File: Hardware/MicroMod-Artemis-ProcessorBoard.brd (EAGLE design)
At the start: 22 x 22 mm, 40 parts, among them J1 MICROMOD-2222, U1 ARTEMIS_MODULESMD, U2 TSV524, U6 CH340E_MSOP10, Y1 32.768kHz

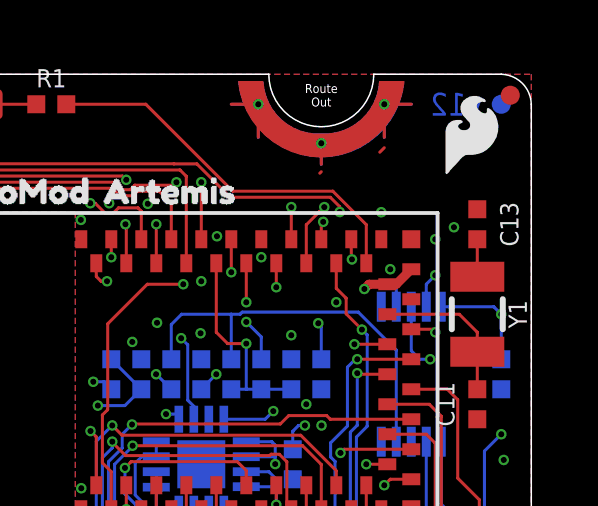
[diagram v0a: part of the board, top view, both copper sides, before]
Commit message: Add missing net to Xtal
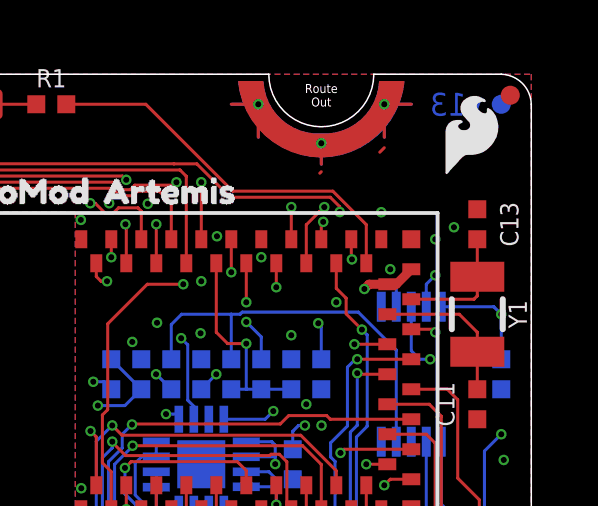
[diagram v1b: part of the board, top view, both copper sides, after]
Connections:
- removed net N$4: U1.XI
- net N$5: now also U1.XI
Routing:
- net N$5: track 1.25 -> 4.13 mm
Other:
- board text added: "v13"
- board text removed: "v12"
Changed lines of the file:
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@@
 <?xml version="1.0" encoding="utf-8"?>
 <!DOCTYPE eagle SYSTEM "eagle.dtd">
-<eagle version="9.6.0">
+<eagle version="9.6.2">
 <drawing>
 <settings>
@@
 <setting verticaltext="up"/>
 </settings>
-<grid distance="0.05" unitdist="inch" unit="inch" style="lines" multiple="1" display="yes" altdistance="0.05" altunitdist="mm" altunit="mm"/>
+<grid distance="0.05" unitdist="inch" unit="inch" style="lines" multiple="1" display="yes" altdistance="0.005" altunitdist="inch" altunit="inch"/>
 <layers>
 <layer number="1" name="Top" color="4" fill="1" visible="yes" active="yes"/>
-<layer number="2" name="Horz" color="1" fill="3" visible="yes" active="yes"/>
-<layer number="15" name="Vert" color="4" fill="6" visible="yes" active="yes"/>
+<layer number="2" name="Horz" color="1" fill="3" visible="no" active="yes"/>
+<layer number="15" name="Vert" color="4" fill="6" visible="no" active="yes"/>
 <layer number="16" name="Bottom" color="1" fill="1" visible="yes" active="yes"/>
 <layer number="17" name="Pads" color="2" fill="1" visible="yes" active="yes"/>
@@
 <layer number="23" name="tOrigins" color="15" fill="1" visible="yes" active="yes"/>
 <layer number="24" name="bOrigins" color="15" fill="1" visible="yes" active="yes"/>
-<layer number="25" name="tNames" color="7" fill="1" visible="yes" active="yes"/>
-<layer number="26" name="bNames" color="7" fill="1" visible="yes" active="yes"/>
-<layer number="27" name="tValues" color="7" fill="1" visible="yes" active="yes"/>
-<layer number="28" name="bValues" color="7" fill="1" visible="yes" active="yes"/>
-<layer number="29" name="tStop" color="7" fill="3" visible="yes" active="yes"/>
-<layer number="30" name="bStop" color="7" fill="6" visible="yes" active="yes"/>
-<layer number="31" name="tCream" color="7" fill="4" visible="yes" active="yes"/>
-<layer number="32" name="bCream" color="7" fill="5" visible="yes" active="yes"/>
-<layer number="33" name="tFinish" color="6" fill="3" visible="yes" active="yes"/>
-<layer number="34" name="bFinish" color="6" fill="6" visible="yes" active="yes"/>
-<layer number="35" name="tGlue" color="7" fill="4" visible="yes" active="yes"/>
-<layer number="36" name="bGlue" color="7" fill="5" visible="yes" active="yes"/>
-<layer number="37" name="tTest" color="7" fill="1" visible="yes" active="yes"/>
-<layer number="38" name="bTest" color="7" fill="1" visible="yes" active="yes"/>
-<layer number="39" name="tKeepout" color="4" fill="11" visible="yes" active="yes"/>
-<layer number="40" name="bKeepout" color="1" fill="11" visible="yes" active="yes"/>
-<layer number="41" name="tRestrict" color="4" fill="10" visible="yes" active="yes"/>
-<layer number="42" name="bRestrict" color="1" fill="10" visible="yes" active="yes"/>
-<layer number="43" name="vRestrict" color="2" fill="10" visible="yes" active="yes"/>
-<layer number="44" name="Drills" color="7" fill="1" visible="yes" active="yes"/>
+<layer number="25" name="tNames" color="7" fill="1" visible="no" active="yes"/>
+<layer number="26" name="bNames" color="7" fill="1" visible="no" active="yes"/>
+<layer number="27" name="tValues" color="7" fill="1" visible="no" active="yes"/>
+<layer number="28" name="bValues" color="7" fill="1" visible="no" active="yes"/>
+<layer number="29" name="tStop" color="7" fill="3" visible="no" active="yes"/>
+<layer number="30" name="bStop" color="7" fill="6" visible="no" active="yes"/>
+<layer number="31" name="tCream" color="7" fill="4" visible="no" active="yes"/>
+<layer number="32" name="bCream" color="7" fill="5" visible="no" active="yes"/>
+<layer number="33" name="tFinish" color="6" fill="3" visible="no" active="yes"/>
+<layer number="34" name="bFinish" color="6" fill="6" visible="no" active="yes"/>
+<layer number="35" name="tGlue" color="7" fill="4" visible="no" active="yes"/>
+<layer number="36" name="bGlue" color="7" fill="5" visible="no" active="yes"/>
+<layer number="37" name="tTest" color="7" fill="1" visible="no" active="yes"/>
+<layer number="38" name="bTest" color="7" fill="1" visible="no" active="yes"/>
+<layer number="39" name="tKeepout" color="4" fill="11" visible="no" active="yes"/>
+<layer number="40" name="bKeepout" color="1" fill="11" visible="no" active="yes"/>
+<layer number="41" name="tRestrict" color="4" fill="10" visible="no" active="yes"/>
+<layer number="42" name="bRestrict" color="1" fill="10" visible="no" active="yes"/>
+<layer number="43" name="vRestrict" color="2" fill="10" visible="no" active="yes"/>
+<layer number="44" name="Drills" color="7" fill="1" visible="no" active="yes"/>
 <layer number="45" name="Holes" color="7" fill="1" visible="yes" active="yes"/>
-<layer number="46" name="Milling" color="3" fill="1" visible="yes" active="yes"/>
-<layer number="47" name="Measures" color="7" fill="1" visible="yes" active="yes"/>
-<layer number="48" name="Document" color="7" fill="1" visible="yes" active="yes"/>
-<layer number="49" name="Reference" color="7" fill="1" visible="yes" active="yes"/>
-<layer number="50" name="dxf" color="7" fill="1" visible="yes" active="yes"/>
+<layer number="46" name="Milling" color="3" fill="1" visible="no" active="yes"/>
+<layer number="47" name="Measures" color="7" fill="1" visible="no" active="yes"/>
+<layer number="48" name="Document" color="7" fill="1" visible="no" active="yes"/>
+<layer number="49" name="Reference" color="7" fill="1" visible="no" active="yes"/>
+<layer number="50" name="dxf" color="7" fill="1" visible="no" active="yes"/>
 <layer number="51" name="tDocu" color="6" fill="1" visible="yes" active="yes"/>
-<layer number="52" name="bDocu" color="7" fill="1" visible="yes" active="yes"/>
+<layer number="52" name="bDocu" color="7" fill="1" visible="no" active="yes"/>
 <layer number="91" name="Nets" color="2" fill="1" visible="no" active="no"/>
 <layer number="92" name="Busses" color="1" fill="1" visible="no" active="no"/>
@@
 <wire x1="0" y1="4.6" x2="0.6" y2="4" width="0.05" layer="20" curve="86.784874"/>
 <rectangle x1="3.1" y1="6.6" x2="6.6" y2="17.3" layer="39"/>
-<text x="19.5" y="21" size="0.762" layer="16" font="vector" ratio="15" rot="SMR0" align="center">v12</text>
+<text x="19.5" y="21" size="0.762" layer="16" font="vector" ratio="15" rot="SMR0" align="center">v13</text>
 <text x="17.78" y="-8.89" size="1.778" layer="51" font="vector" ratio="15">N. Seidle</text>
 <wire x1="13.25" y1="22" x2="16.75" y2="22" width="0.05" layer="20" curve="180"/>
@@
 <wire x1="15.15594375" y1="3.7286" x2="15.8734" y2="4.44605625" width="0.1016" layer="16"/>
 </signal>
-<signal name="N$4">
-<contactref element="U1" pad="XI"/>
-</signal>
 <signal name="N$5">
 <contactref element="Y1" pad="P$1"/>
 <contactref element="C13" pad="2"/>
 <wire x1="20.2" y1="15.25" x2="20.2" y2="16.5" width="0.1016" layer="1"/>
-</signal>
-<signal name="N$6">
+<contactref element="U1" pad="XI"/>
+<wire x1="18" y1="14.5" x2="20.088" y2="14.5" width="0.1016" layer="1"/>
+<wire x1="20.2" y1="14.612" x2="20.2" y2="15.25" width="0.1016" layer="1"/>
+<wire x1="20.088" y1="14.5" x2="20.2" y2="14.612" width="0.1016" layer="1"/>
 </signal>
 <signal name="SCALED_BATT_VIN/3">

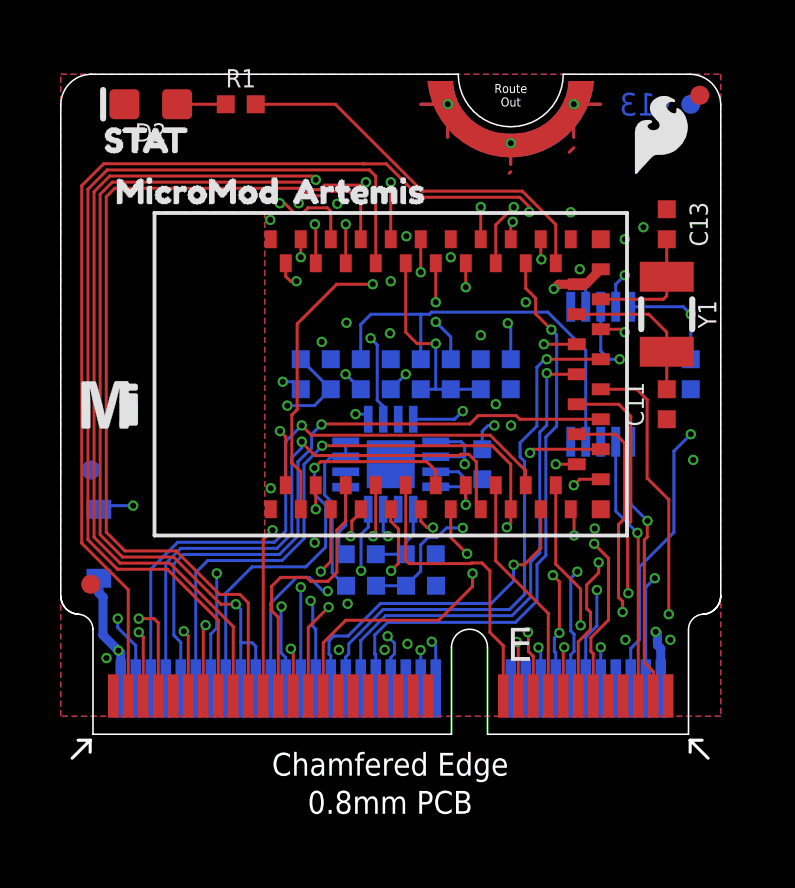
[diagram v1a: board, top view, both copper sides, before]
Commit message: Fix SDA1/SCL1, CS1, and VIN/3 incorrect pin locations.
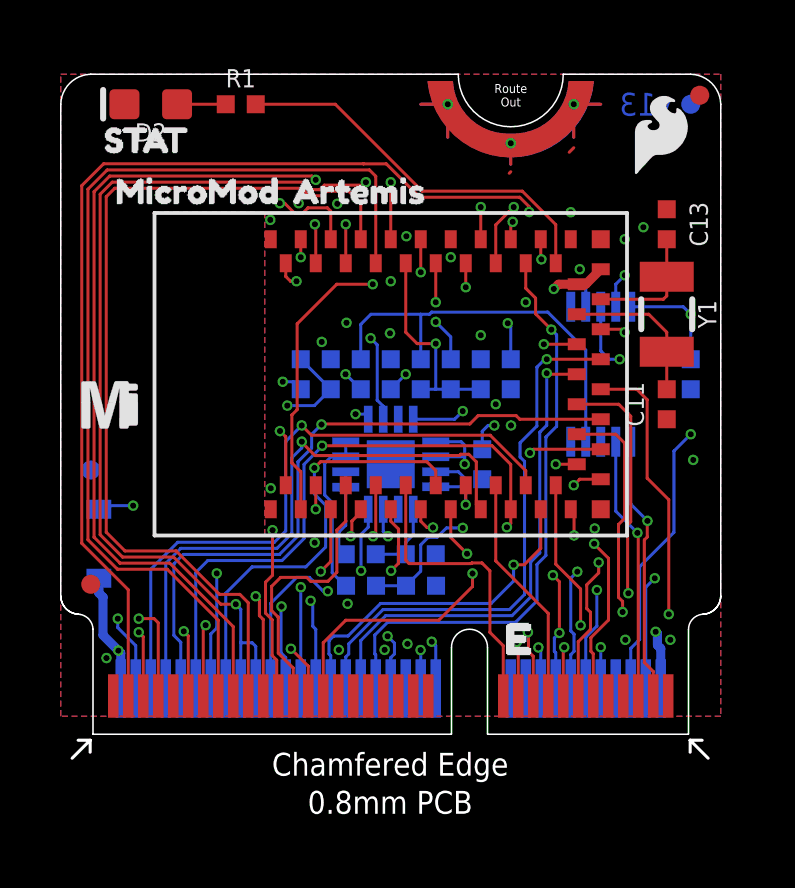
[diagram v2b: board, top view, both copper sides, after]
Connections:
- net BATT_VIN/3: now also J1.49; no longer J1.51
- net SCL1: now also J1.53; no longer J1.55
- net SDA1: now also J1.51; no longer J1.53
- net SPI_!CS!1: now also J1.55; no longer J1.49
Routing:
- net SPI_!CS!1: track 22.9 -> 28.2 mm
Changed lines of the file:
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@@
 <?xml version="1.0" encoding="utf-8"?>
 <!DOCTYPE eagle SYSTEM "eagle.dtd">
-<eagle version="9.6.2">
+<eagle version="9.6.0">
 <drawing>
 <settings>
@@
 <setting verticaltext="up"/>
 </settings>
-<grid distance="0.05" unitdist="inch" unit="inch" style="lines" multiple="1" display="yes" altdistance="0.005" altunitdist="inch" altunit="inch"/>
+<grid distance="1" unitdist="mm" unit="mm" style="lines" multiple="1" display="yes" altdistance="0.1" altunitdist="mm" altunit="mm"/>
 <layers>
 <layer number="1" name="Top" color="4" fill="1" visible="yes" active="yes"/>
 <layer number="2" name="Horz" color="1" fill="3" visible="no" active="yes"/>
-<layer number="15" name="Vert" color="4" fill="6" visible="no" active="yes"/>
+<layer number="15" name="Vert" color="4" fill="6" visible="yes" active="yes"/>
 <layer number="16" name="Bottom" color="1" fill="1" visible="yes" active="yes"/>
 <layer number="17" name="Pads" color="2" fill="1" visible="yes" active="yes"/>
@@
 </signal>
 <signal name="BATT_VIN/3">
-<contactref element="J1" pad="51"/>
 <contactref element="R2" pad="2"/>
-<wire x1="7.75" y1="1.275" x2="7.75" y2="2.7714" width="0.1016" layer="1"/>
-<wire x1="7.75" y1="2.7714" x2="7.6714" y2="2.85" width="0.1016" layer="1"/>
 <via x="7.6714" y="2.85" extent="1-16" drill="0.2"/>
 <wire x1="7.68654375" y1="4.3940625" x2="7.68654375" y2="2.86514375" width="0.1016" layer="15"/>
@@
 <wire x1="7.2233625" y1="11.59128125" x2="7.2233625" y2="10.66905625" width="0.1016" layer="15"/>
 <wire x1="7.2233625" y1="10.66905625" x2="7.6714" y2="10.22101875" width="0.1016" layer="15"/>
+<contactref element="J1" pad="49"/>
+<wire x1="8.25" y1="1.275" x2="8.25" y2="2.2714" width="0.1016" layer="1"/>
+<wire x1="8.25" y1="2.2714" x2="7.6714" y2="2.85" width="0.1016" layer="1"/>
 </signal>
 <signal name="ADC0">
@@
 <wire x1="12" y1="7.1" x2="12.207646875" y2="6.892353125" width="0.1016" layer="1"/>
 <wire x1="12" y1="7.5" x2="12" y2="7.1" width="0.1016" layer="1"/>
-<wire x1="6.75" y1="6.49206875" x2="7.05953125" y2="6.8016" width="0.1016" layer="1"/>
 <via x="7.05953125" y="6.8016" extent="1-16" drill="0.2"/>
-<contactref element="J1" pad="55"/>
-<wire x1="6.75" y1="1.275" x2="6.75" y2="6.49206875" width="0.1016" layer="1"/>
+<wire x1="7.05953125" y1="5.3016" x2="7.05953125" y2="6.8016" width="0.1016" layer="1"/>
+<wire x1="7.05953125" y1="5.3016" x2="6.82615" y2="5.06821875" width="0.1016" layer="1"/>
 <wire x1="12.407646875" y1="6.938721875" x2="12.407646875" y2="6.892353125" width="0.1016" layer="2"/>
 <wire x1="7.05953125" y1="6.8376125" x2="7.05953125" y2="6.8016" width="0.1016" layer="2"/>
@@
 <wire x1="8.94763125" y1="7.335" x2="12.01136875" y2="7.335" width="0.1016" layer="2"/>
 <wire x1="12.01136875" y1="7.335" x2="12.407646875" y2="6.938721875" width="0.1016" layer="2"/>
+<contactref element="J1" pad="53"/>
+<wire x1="7.25" y1="1.275" x2="7.2" y2="1.325" width="0.1016" layer="1"/>
+<wire x1="7.2" y1="1.325" x2="7.2" y2="2.46931875" width="0.1016" layer="1"/>
+<wire x1="7.2" y1="2.46931875" x2="7.0468" y2="2.62251875" width="0.1016" layer="1"/>
+<wire x1="7.0468" y1="3.81701875" x2="6.82615" y2="4.03766875" width="0.1016" layer="1"/>
+<wire x1="7.0468" y1="2.62251875" x2="7.0468" y2="3.81701875" width="0.1016" layer="1"/>
+<wire x1="6.82615" y1="4.03766875" x2="6.82615" y2="5.06821875" width="0.1016" layer="1"/>
 </signal>
 <signal name="SDA1">
@@
 <wire x1="7.02935" y1="4.92935" x2="7.3286" y2="5.2286" width="0.1016" layer="1"/>
 <wire x1="7.3286" y1="5.2286" x2="8.1996875" y2="5.2286" width="0.1016" layer="1"/>
-<contactref element="J1" pad="53"/>
-<wire x1="7.25" y1="1.275" x2="7.25" y2="3.9011875" width="0.1016" layer="1"/>
 <wire x1="8.3308875" y1="5.0974" x2="8.9031125" y2="5.0974" width="0.1016" layer="1"/>
 <wire x1="8.1996875" y1="5.2286" x2="8.3308875" y2="5.0974" width="0.1016" layer="1"/>
@@
 <wire x1="9.2032" y1="5.3974875" x2="9.2032" y2="6.8032" width="0.1016" layer="1"/>
 <wire x1="9.2032" y1="6.8032" x2="9.5" y2="7.1" width="0.1016" layer="1"/>
+<contactref element="J1" pad="51"/>
+<wire x1="7.75" y1="1.275" x2="7.75" y2="2.2066875" width="0.1016" layer="1"/>
+<wire x1="7.25" y1="2.7066875" x2="7.25" y2="3.9011875" width="0.1016" layer="1"/>
+<wire x1="7.75" y1="2.2066875" x2="7.25" y2="2.7066875" width="0.1016" layer="1"/>
 </signal>
 <signal name="SDIO_DATA1">
@@
 <signal name="SPI_!CS!1">
 <contactref element="U1" pad="D41"/>
-<via x="8.9286" y="4.23654375" extent="1-16" drill="0.2"/>
-<wire x1="8.25" y1="3.55794375" x2="8.9286" y2="4.23654375" width="0.1016" layer="1"/>
 <wire x1="14" y1="16.5" x2="14" y2="17.5714" width="0.1016" layer="1"/>
 <via x="14" y="17.5714" extent="1-16" drill="0.2"/>
@@
 <wire x1="9.217896875" y1="17.646815625" x2="9.2933125" y2="17.5714" width="0.1016" layer="2"/>
 <wire x1="9.117896875" y1="17.582103125" x2="9.217896875" y2="17.682103125" width="0.1016" layer="15"/>
-<contactref element="J1" pad="49"/>
-<wire x1="8.25" y1="1.275" x2="8.25" y2="3.55794375" width="0.1016" layer="1"/>
 <wire x1="9.16426875" y1="11.8638875" x2="9.16426875" y2="16.13573125" width="0.1016" layer="15"/>
 <wire x1="9.117896875" y1="16.182103125" x2="9.117896875" y2="17.582103125" width="0.1016" layer="15"/>
@@
 <wire x1="8.9286" y1="4.23654375" x2="9.2936" y2="4.60154375" width="0.1016" layer="15"/>
 <wire x1="9.2936" y1="4.60154375" x2="9.2936" y2="11.72815625" width="0.1016" layer="15"/>
+<contactref element="J1" pad="55"/>
+<via x="6.49755" y="4.5997875" extent="1-16" drill="0.2"/>
+<wire x1="6.75" y1="1.275" x2="6.75" y2="3.82645" width="0.1016" layer="1"/>
+<wire x1="6.75" y1="3.82645" x2="6.62295" y2="3.9535" width="0.1016" layer="1"/>
+<wire x1="6.62295" y1="4.4743875" x2="6.49755" y2="4.5997875" width="0.1016" layer="1"/>
+<wire x1="6.62295" y1="3.9535" x2="6.62295" y2="4.4743875" width="0.1016" layer="1"/>
+<wire x1="7.3428" y1="2.7138875" x2="7.5352875" y2="2.5214" width="0.1016" layer="15"/>
+<wire x1="6.49755" y1="4.5997875" x2="7.3428" y2="3.7545375" width="0.1016" layer="15"/>
+<wire x1="7.3428" y1="3.7545375" x2="7.3428" y2="2.7138875" width="0.1016" layer="15"/>
+<wire x1="8.9286" y1="3.3286" x2="8.9286" y2="4.23654375" width="0.1016" layer="15"/>
+<wire x1="7.5352875" y1="2.5214" x2="8.1214" y2="2.5214" width="0.1016" layer="15"/>
+<wire x1="8.1214" y1="2.5214" x2="8.9286" y2="3.3286" width="0.1016" layer="15"/>
 </signal>
 <signal name="CLKOUT">

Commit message: Roll version to v1.4
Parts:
- moved FRAME1 39.8 mm to (30.9, -8.89), flipped to the bottom
- moved LOGO4 27.1 mm to (-2.54, 50.8), flipped to the bottom
- moved FD2 20.6 mm to (0.70, 21.3), flipped to the bottom
- moved U$4 20.6 mm to (21.3, 19.8), flipped to the bottom
- moved C17 20.0 mm to (1.00, 12.0), flipped to the top
- moved FD1 20.0 mm to (21.0, 5.00), flipped to the bottom
- moved FD3 20.0 mm to (1.00, 21.0), flipped to the top
- moved FD4 20.0 mm to (21.0, 8.81), flipped to the top
- moved U$3 19.8 mm to (20.9, 18.1), flipped to the bottom
- moved D7 19.5 mm to (20.7, 6.35), flipped to the top
- moved U$7 19.0 mm to (1.50, 5.90), flipped to the top
- moved U$1 18.8 mm to (20.4, 11.0), flipped to the bottom
- moved C11 18.4 mm to (1.80, 11.0), flipped to the bottom
- moved C13 18.4 mm to (1.80, 17.0), flipped to the bottom
- moved Y1 18.4 mm to (1.80, 14.0), flipped to the bottom
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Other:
- outline, holes or cut-outs redrawn
- board text added: "v14"
- board text removed: "v13"
